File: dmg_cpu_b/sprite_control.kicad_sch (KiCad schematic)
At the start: 136 parts

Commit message: Changes made on review.
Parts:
- added ATAR: INVERTER_A, symbol DMG_CPU_Cells:INVERTER_A
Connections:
- net RESET_VIDEO: now also ATAR.2
- net ~{RESET_VIDEO} renamed ~{PPU_RESET}
- net ~{PPU_RESET}: now also ATAR.1
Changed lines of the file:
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@@
+    (stroke (width 0) (type default) (color 0 0 0 0))
+  )
+  (wire (pts (xy 127.635 159.385) (xy 140.97 159.385))
     (stroke (width 0) (type default) (color 0 0 0 0))
   )
@@
     (stroke (width 0) (type default) (color 0 0 0 0))
   )
+  (wire (pts (xy 36.195 53.34) (xy 36.195 55.88))
+    (stroke (width 0) (type default) (color 0 0 0 0))
+  )
   (wire (pts (xy 119.38 219.075) (xy 118.11 219.075))
     (stroke (width 0) (type default) (color 0 0 0 0))
@@
     (stroke (width 0) (type default) (color 0 0 0 0))
   )
-  (wire (pts (xy 36.195 58.42) (xy 37.465 58.42))
+  (wire (pts (xy 22.86 58.42) (xy 37.465 58.42))
     (stroke (width 0) (type default) (color 0 0 0 0))
   )
@@
     (stroke (width 0) (type default) (color 0 0 0 0))
   )
+  (wire (pts (xy 36.195 55.88) (xy 37.465 55.88))
+    (stroke (width 0) (type default) (color 0 0 0 0))
+  )
   (wire (pts (xy 170.815 99.06) (xy 170.815 139.7))
     (stroke (width 0) (type default) (color 0 0 0 0))
@@
     (stroke (width 0) (type default) (color 0 0 0 0))
   )
-  (wire (pts (xy 36.195 55.88) (xy 37.465 55.88))
+  (wire (pts (xy 34.925 53.34) (xy 36.195 53.34))
     (stroke (width 0) (type default) (color 0 0 0 0))
   )
@@
   )
   (wire (pts (xy 167.64 226.695) (xy 193.675 226.695))
+    (stroke (width 0) (type default) (color 0 0 0 0))
+  )
+  (wire (pts (xy 100.965 159.385) (xy 114.935 159.385))
     (stroke (width 0) (type default) (color 0 0 0 0))
   )
@@
     (effects (font (size 1.27 1.27)) (justify left bottom))
   )
+  (label "~{PPU_RESET}" (at 22.86 58.42 0)
+    (effects (font (size 1.27 1.27)) (justify left bottom))
+  )
   (label "SAVE_SPRITE_NUM_0" (at 269.24 66.04 180)
     (effects (font (size 1.27 1.27)) (justify right bottom))
@@
     (effects (font (size 1.27 1.27)) (justify right bottom))
   )
+  (label "~{PPU_RESET}" (at 100.965 159.385 0)
+    (effects (font (size 1.27 1.27)) (justify left bottom))
+  )
   (label "SAVE_SPRITE_X_2" (at 269.24 133.35 180)
     (effects (font (size 1.27 1.27)) (justify right bottom))
@@
     (effects (font (size 1.27 1.27)) (justify right bottom))
   )
+  (label "RESET_VIDEO" (at 140.97 159.385 180)
+    (effects (font (size 1.27 1.27)) (justify right bottom))
+  )
   (label "SAVE_SPRITE_Y_9" (at 398.145 240.03 180)
     (effects (font (size 1.27 1.27)) (justify right bottom))
@@
     (effects (font (size 1.27 1.27)) (justify right))
   )
-  (hierarchical_label "RESET_VIDEO" (shape input) (at 137.795 259.715 180)
-    (effects (font (size 1.27 1.27)) (justify right))
-  )
   (hierarchical_label "OAM_RENDERING" (shape output) (at 114.935 204.47 0)
     (effects (font (size 1.27 1.27)) (justify left))
@@
     (effects (font (size 1.27 1.27)) (justify left))
   )
-  (hierarchical_label "PPU_4MHz" (shape input) (at 36.195 55.88 180)
+  (hierarchical_label "PPU_4MHz" (shape input) (at 34.925 53.34 180)
     (effects (font (size 1.27 1.27)) (justify right))
   )
@@
     (effects (font (size 1.27 1.27)) (justify right))
   )
-  (hierarchical_label "~{RESET_VIDEO}" (shape input) (at 36.195 58.42 180)
+  (hierarchical_label "~{PPU_RESET}" (shape input) (at 100.965 159.385 180)
     (effects (font (size 1.27 1.27)) (justify right))
   )
@@
       (effects (font (size 1.27 1.27)) hide)
     )
+    (pin "1")
+    (pin "2")
+  )
+  (symbol (lib_id "DMG_CPU_Cells:INVERTER_A") (at 121.285 159.385 0) (unit 1)
+    (in_bom yes) (on_board yes) (fields_autoplaced)
+    (property "Reference" "ATAR" (id 0) (at 121.285 151.8752 0))
+    (property "Value" "INVERTER_A" (id 1) (at 121.285 154.4121 0))
+    (property "Footprint" "" (id 2) (at 118.745 159.385 0)
+      (effects (font (size 1.27 1.27)) hide)
+    )
+    (property "Datasheet" "http://iceboy.a-singer.de/doc/dmg_cells.html#inv_a" (id 3) (at 122.555 167.005 0)
+      (effects (font (size 1.27 1.27)) hide)
+    )

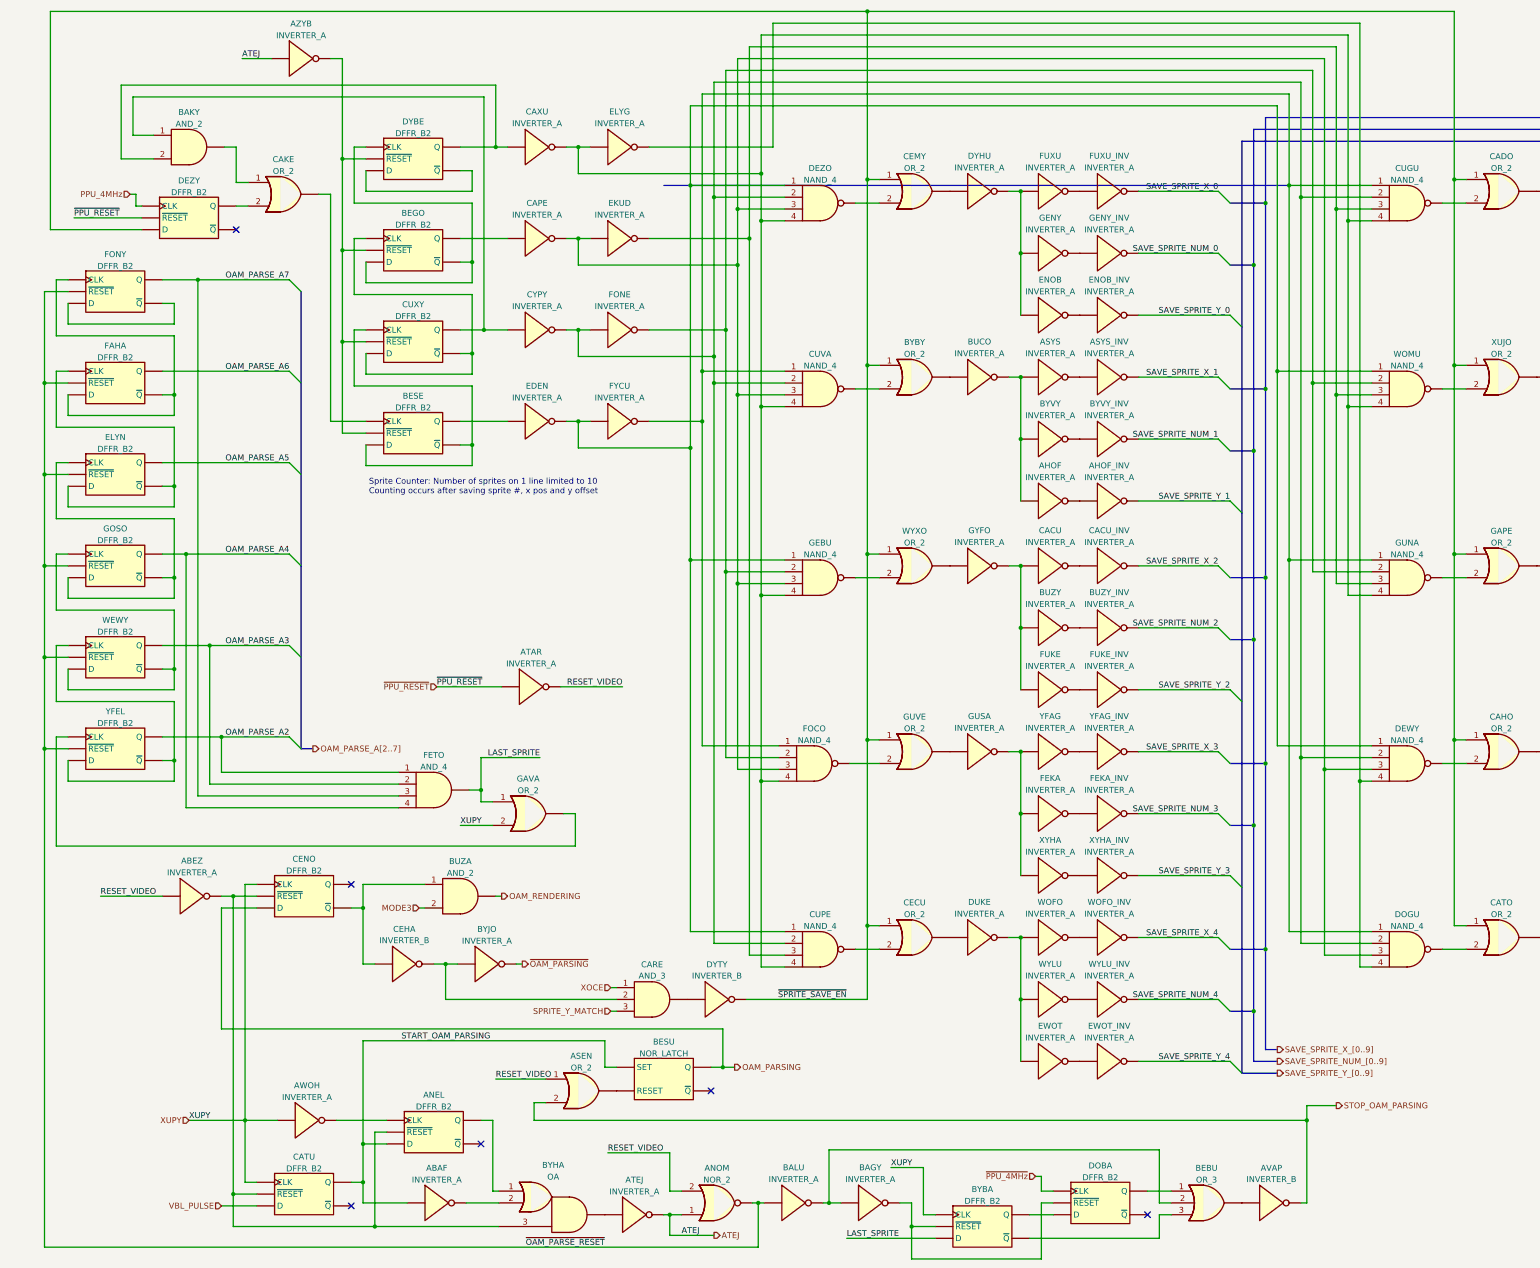
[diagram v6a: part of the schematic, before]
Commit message: Elements from sptite control sheet moved to lcd sheet.
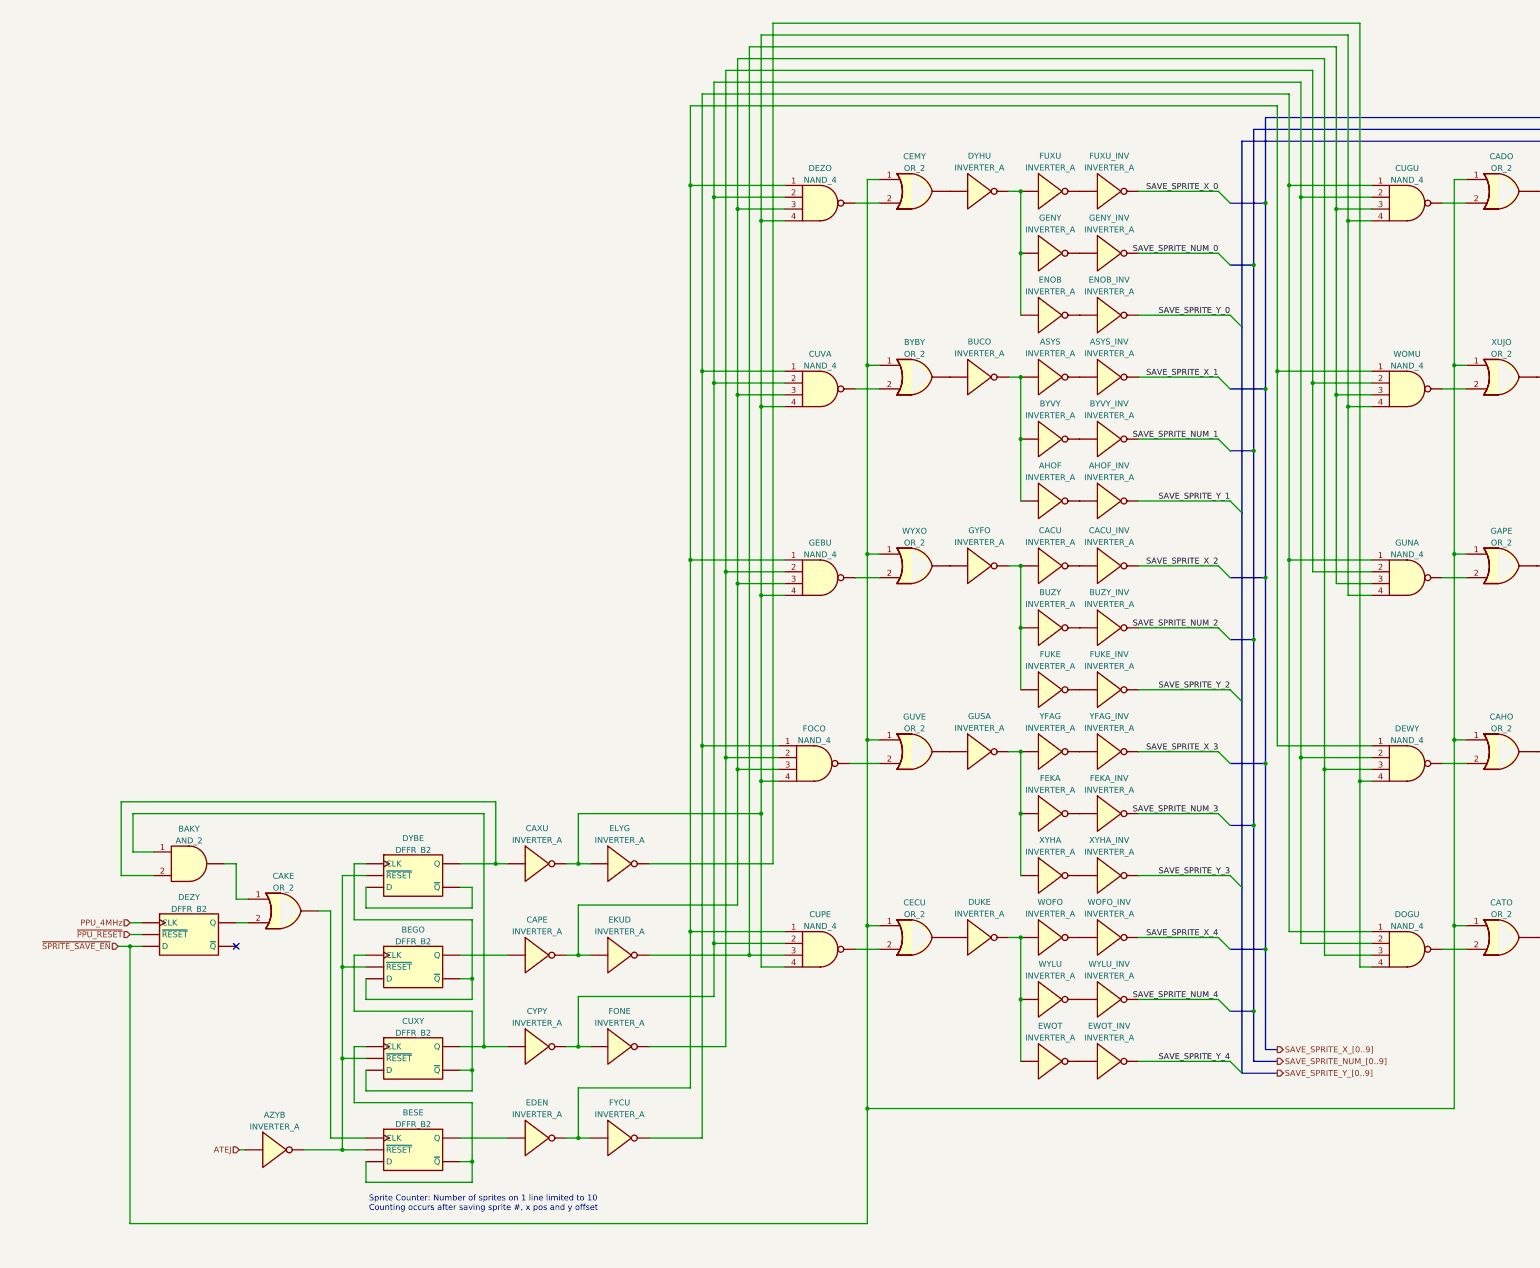
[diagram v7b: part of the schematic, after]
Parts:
- removed ABAF, ABEZ, ATAR, ATEJ, AWOH, BAGY, BALU, BYJO: INVERTER_A, symbol DMG_CPU_Cells:INVERTER_A
- removed ANEL, BYBA, CATU, CENO, DOBA, ELYN, FAHA, FONY, GOSO, WEWY, YFEL: DFFR_B2, symbol DMG_CPU_Cells:DFFR_B2
- removed ANOM: NOR_2, symbol DMG_CPU_Cells:NOR_2
- removed ASEN, GAVA: OR_2, symbol DMG_CPU_Cells:OR_2
- removed AVAP, CEHA, DYTY: INVERTER_B, symbol DMG_CPU_Cells:INVERTER_B
- removed BEBU: OR_3, symbol DMG_CPU_Cells:OR_3
- removed BESU: NOR_LATCH, symbol DMG_CPU_Cells:NOR_LATCH
- removed BUZA: AND_2, symbol DMG_CPU_Cells:AND_2
- removed BYHA: OA, symbol DMG_CPU_Cells:OA
- removed CARE: AND_3, symbol DMG_CPU_Cells:AND_3
- removed FETO: AND_4, symbol DMG_CPU_Cells:AND_4
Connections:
- no-connect marks 6 -> 1
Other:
- moved on the sheet: AZYB, BAKY, BEGO, BESE, CAKE, CAPE, CAXU, CUXY, CYPY, DEZY, DYBE, EDEN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
